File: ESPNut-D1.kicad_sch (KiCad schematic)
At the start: 53 parts, among them J1 USB_C_Receptacle_USB2.0, J2 ESP_CONN, J3 USB_PADS, J4 ESP_PROG, Q1 BC817, Q2 BC817, Q3 Si2302CDS, SW1 ESP_RST, SW2 ESP_BOOT, SW3 ESP_VDD_SW, SW4 POW_CTRL, U1 CH340G, U2 MIC5219-3.3YM5, Y1 12MHz

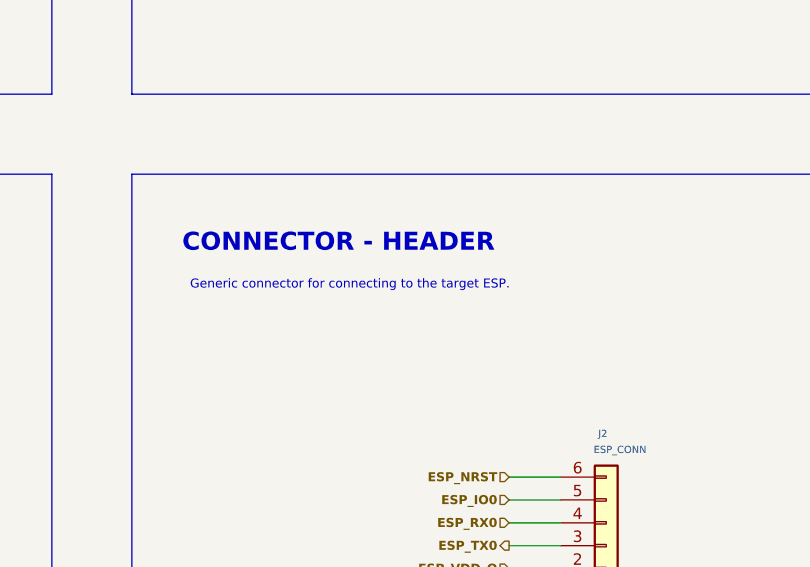
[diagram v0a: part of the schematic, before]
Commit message: Added fiducial
- Added fiducial to the front side.
- Generated new manufacturing files.
- Updated Readme.
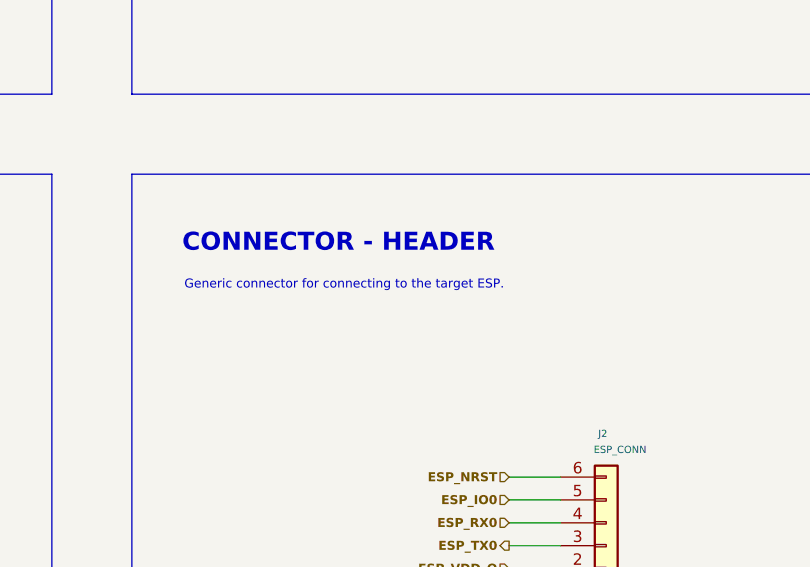
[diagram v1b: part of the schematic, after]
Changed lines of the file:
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@@
 	(title_block
 		(title "ESPNut-D1")
-		(date "2025-04-11")
+		(date "2025-04-23")
 		(rev "0.1")
 		(company "CIRCUITSTATE Electronics LLP (www.circuitstate.com)")
@@
 	(text_box "Generic connector for connecting to the target ESP."
 		(exclude_from_sim no)
-		(at 213.995 120.015 0)
+		(at 213.36 120.015 0)
 		(size 43.815 2.54)
 		(margins 0.7499 0.7499 0.7499 0.7499)
@@
 			"AGUAQQBkACsARABqADEAQQBKAHkAVwAzAFcAYgAxAEUAQgBFAC8ASAA3AG4ATQB6AGYARwBUAEEA"
 			"TQBBAFQAQgBkAGsAQQBBAEEAQQBBAEEAQQBBAEEAQQBBAEEAQQBBAEEAQQBBAEEAQQBCAHcASABt"
-			"ADYAVAB1AGQAawByAFgAeQBzAFMAMQA5AGYASgBmAFEANgBTAEwAQwBIACsATgBDACsAcgBqAA=="
+			"ADYAVAB1AGQAawByAFgAeQBzAFMAMQA5AGYASgBmAFEANgBTAEwAQwBIACsATgBDACsAcgBqAC8A"
+			"VAAvAEIAawBBAFAAZABwAHYAVgBRADMAVAA3AGUAMAB6AEUAWQBhAFgAYQBBAFAAQwBxAEgANgBj"
+			"AGUAQQBBAEEAQQBBAEEAQQBBAEEAQQBBAEEAQQBBAEEAQQBBAEEAQQBBAEEARQBqADcARwBoAEcA"
+			"ZgBFADcAbABGAC8ATAA0AGMATgAzAE4AZAAwADIAMgBjAHcAKwB3ADIAcQA0AGQANQBXAGQAMQBH"
+			"AHgASwBjADkAMABTAEkAaQB0AHQAOQA4AGIAcABIAGMAbwArADQANgAxADAAQwBjAG0AVABQADcA"
+			"VgB0AE4AdABuAE0ATwA4AGwAVABPAGIAbAA5AFUAcwBuAGcAbwBUAFAANwA0AFMAdQA5AHQAdABW"
+			"AHUAdQBoAFoANABFADkAcgBpAFAAaQBwADIAVAAyAGEAbAA1AFcATgAyADAAaABIAFEAQgBrAEwA"
+			"VAB0AGsAYgA5AG8ASABPAEUAeABtAFgAbABaADMARQBmAEgAbgBaAEwAdwBJAHAAYQB0ADAANQBP"
+			"ADgASwAwAEkAdAAxADUAUAA4AGUAOAB4AGcAUgBOADQATgBOAEEAcwBDADcAOQBjAFAAVQBBAHcA"
+			"QQBBAEEAQQBBAEEAQQBBAEEAQQBBAEEAQQBBAEEAQQBBAEEAQQBBAEIAcABUAFQASwAzAGUAUAA2"
+			"AGIAZQBWAGsAVgBpAFcAdAB1AFIAeQA3AHEAcgBCAE8AWgA0AHYAbAB2ADIAdgBLAHIARAA0AG4A"
+			"cgBiAHIAdQBQAE0ANQBnAG0AbQBWAHMAOAAvADQAMAB6AG0AMQBTAFQAegBDADIAZQAvADgAYQBa"
+			"AEQAYQBhAE8AaQBMADkARgB4AEYAOQBlACsAZgBqAEgAdgBLAHoAVwBJADgAMABUADgAWABvAEIA"
+			"SAArADkAVQBXADAATAA2AFMAegBMACsASQBTAEsAdQBCAGgAdQBtAG0ANAA5AFQARAA4AEMAZwBI"
+			"AHEAYwBlAGcASABkAHAATQBmAFUAQQBiADEAaQBSAHoATgAxAE8AWABZADQAZAA4AGQAdgBQAHgA"
+			"dQB3ADkANAAzAEsANABTAFgAagBEADYAdgBCADMAaABYAFAAMQBjAGUAbwBCAGUATgBJACsAKwBP"
+			"AHEAdgBzAGYAKwArADgAVABZAGkAQwBnAC8ANQBBAFcAQQBJAFAAMAA0ADkAQQBBAEEAQQBBAEEA"
+			"QQBBAEEAQQBBAEEAQQBBAEEAQQBBAEEAQQBBAEEASgBEAFcASgBIAE8ATABiADMANQBmAEoASwA2"
+			"AHAATwA4AHoAUgBoAHoAbwBpAC8AcgB3AG4AVQAzAHoAegArADEAbQBIAHQAVQA5AEYAawA4AHQA"
+			"cgBrAFkAagBmAHQAawBXADYAWQA2AHMAVABtAGUATABaAGYAOAA4AHkAaQAzAFkAcwBGAEIAeABE"
+			"AGsAdwBrADUAcwA1AFAAUwBaAEUATABPADcATQAyAHAATwAyAFMATABnAFcAWQA0AHgATABKAEQA"
+			"OQBtAEcAZwBHAFcAagB0AE4AcQB0AHQANQBJAHQAQQBMACsAWgBsAGQAVABuAFEASwBIAFcASABi"
+			"AEQASABRAEQASQBkAFkAZABzAGcAKwA5AEwAVABuAFgAVABMADMAKwBZAFMASwBIAEkAdABrAHIA"
+			"aAA1AHcAQgBvAFoAMwBqAHEAWABDAHkAMgBRAHUAOAB6AEEAUwBXAHUAMAA5ADUAMABVAHkAWABn"
+			"ADgAMwB5AGMARwAyAHkAZAB6AEYAcgAvAGYAWABjAEkATABxAEQAdABsAGkAbwBCAGsATwBzAGUA"
+			"eQBRAGYAZQBoAGgAdgA3AHAARAB0AHUAaABoAHYANwA0AHMATwAyAFMAYgBnAFcAWQBBAGcASABk"
+			"AEwAUQBUAFkAQQBBAEEAQQBBAEEAQQBBAEEAQQBBAEEAQQBBAEEAQQBBAEEAQQBDAGMAbAB6AHEA"
+			"WgBXADcAUwAvAEYAagAyAHUAMgBiAGYATQB2AHMAVwB6AC8ALwA2AFUAeQBIADgAOQBhAEoASgBo"
+			"ADEAYwBuAGMAbwB2ADIAMQA2AEgASABOAHYAbQBYADIATABaADcAOQB0AHoAUAByAHYAbQBiAGYA"
+			"TQB2AHMAVwB6AC8ANwA3AFgATQArAHMARAAzAGMAZABzAHAAYwBEAHoAWABDAEkAcQAyAHgAdwB0"
+			"ADEAbgBWAHcANAAzAEIATQA5AGMARABaAGIAdQA0ADYANQBDADkASABHAGkARwBRADEAeABsAGcA"
+			"egAyACsAbgA1AHMATwAyAFcAVgBQAGUAeAA2AHMATABWAFgALwBrAEkAegBmAEQAVABjAEoASQAy"
+			"AGkAUwB1AFkAdgBrAHcAegBvAEcATgBTACsAcgBXAFUAUgA4AFQAcwBhAGIANABTAFoANQBrADUA"
+			"WQBkAHMAdQB1AEIAWgBqAGoARwB1AGsATwAyAEcARwBnAEcATwBOAFoAZABoACsAegBsAFEARABN"
+			"AGMANABpAG8AYgA3AE8AbgBlADYAcQA1AEQAOQByAEsASAAvAGYAcAB5AG0AYwB6AGQAVAAvAFQA"
+			"ZwBLAHcAQgA0ADAAeABSAGsAQQB3AEEAQQBBAEEAQQBBAEEAQQBBAEEAQQBBAEEAQQBBAEEAQQBB"
+			"AHcASABsAHAAawByAGwAWgArADIAdQBSAHkATgBZAEgAegBOAEcASAB6AEwANgBmADUAbQBYAA=="
 		)
 	)

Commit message: New Revision `R0.2`
- Schematic
  - Deleted the Mosfet based power control circuit.
    - Replaced it with `AP22804AW5` based circuit.
    - Not because it is not working, but because a proper load switch is more reliable.
  - Added 6-pin `SM06B-SRSS-TB` JST-SH connector for target ESP.
    - The THT pin-headers will be changes to SMD one and placed on the back side.
  - Added `PCM12SMTR` SPDT switch for ESP voltage selection.
    - Removed the 3-pin solder jumper.
- PCB
  - Imported all changes to the PCB.
  - Deleted all existing tracks and vias.
  - Rearranged the components.
  - Updated label styles and placements.
  - There is now more alignment and symmetry.
  - Routing pending.
- New Revision `R0.2`.
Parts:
- removed D1, D4: RB751V40, Diode_SMD:D_SOD-323_HandSoldering, symbol Diode:MBR340
- removed D5: ESP_PWR, LED_SMD:LED_0603_1608Metric, symbol Device:LED
- removed JP3: VDD_CTRL_BYP, CSE_Solder-Jumper:Solder-Jumper-1x2_P1.3mm_Open_Rounded_1.0x1.2mm, symbol Jumper:SolderJumper_2_Open
- removed JP4: ESPV_SEL, CSE_Solder-Jumper:Solder-Jumper-1x3_P1.3mm_Open_Rounded_1.0x1.5mm_Labels, symbol Jumper:SolderJumper_3_Open
- removed Q3: Si2302CDS, Package_TO_SOT_SMD:SOT-23, symbol PCM_Transistor_MOSFET_AKL:Si2302CDS
- removed R8: 5.1K, Resistor_SMD:R_0402_1005Metric, symbol Device:R_Small
- removed R9: 220R, Resistor_SMD:R_0402_1005Metric, symbol Device:R_Small
- added D3: ESP_PWR, LED_SMD:LED_0603_1608Metric, symbol Device:LED
- added J3: ESP_CONN, CSE_Connector_JST_SH:JST_SH_SM06B-SRSS-TB_1x06-1MP_P1.00mm_Horizontal, symbol Connector_Generic:Conn_01x06
- added JP1: RST_PUE, CSE_Solder-Jumper:Solder-Jumper-1x2_P1.3mm_Open_Rounded_1.0x1.2mm, symbol Jumper:SolderJumper_2_Open
- added JP2: BT_PUE, CSE_Solder-Jumper:Solder-Jumper-1x2_P1.3mm_Open_Rounded_1.0x1.2mm, symbol Jumper:SolderJumper_2_Open
- added JP6: ESP_VDD_SW, CSE_Solder-Jumper:Solder-Jumper-1x2_P1.3mm_Open_Rounded_1.0x1.2mm, symbol Jumper:SolderJumper_2_Open
- added R10, R12, R3, R4: 10K, Resistor_SMD:R_0402_1005Metric, symbol Device:R_Small
- added R11, R13: 220R, Resistor_SMD:R_0402_1005Metric, symbol Device:R_Small
- added SW4: ESPV_SEL, Button_Switch_SMD:SW_SPDT_PCM12, symbol Switch:SW_SPDT
- added U3: AP22804AW5, Package_TO_SOT_SMD:SOT-23-5, symbol Power_Management:AP22804AW5
- J2: footprint Connector_PinHeader_2.54mm:PinHeader_1x06_P2.54mm_Vertical -> CSE_Solderpads:Solderpad_1x06_P2.54mm_Rounded_Rectangle
- JP5: value ESP_VDD_SW -> VDD_CTRL_BYP
- renumbered D2 to D1, D3 to D2, J3 to J4, J4 to J5, JP1 to JP3, JP2 to JP4, JP6 to JP7, R3 to R5, R4 to R6, R5 to R7, R6 to R8, R7 to R9, SW4 to SW5, TP8 to TP1, TP9 to TP2, TP1 to TP3, TP2 to TP4, TP3 to TP5, TP4 to TP6, TP5 to TP7, TP6 to TP8, TP7 to TP9
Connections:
- net +3V3: now also R3.1, R4.1, SW4.3 (C)
- net DTR: now also R11.2
- net ESP_IO0: now also Q2.3 (C), J3.5 (Pin_5), JP2.1 (A)
- net ESP_NRST: now also Q1.3 (C), J3.6 (Pin_6), JP1.1 (A)
- net ESP_RX0: now also J3.4 (Pin_4)
- net ESP_TX0: now also J3.3 (Pin_3)
- net ESP_VDD_I: now also JP5.2 (B), R10.2, R12.2, SW4.2 (B), U3.5 (IN)
- net ESP_VDD_O: now also D3.2 (A), J3.2 (Pin_2), JP6.1 (A); no longer JP5.1 (A)
- net GND: now also J3.1 (Pin_1), R13.1, U3.2 (GND)
- net VBUS: now also SW4.1 (A)
- net at TP11.1: now also D3.1 (K), R13.2
- net at JP7.2 (B), SW5.2: now also R10.1, R11.1, U3.4 (EN)
- net at SW3.1 (A): now also JP5.1 (A), JP6.2 (B), U3.1 (OUT); no longer JP5.2 (B)
- new net: JP2.2 (B), R4.2
- new net: R12.1, U3.3 (~{FLG})
- new net: JP1.2 (B), R3.2
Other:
- note added: "CH340G/C"
- note added: "JST-SH"
- note added: "Pin-Header"
- note removed: "CH340G"
- note removed: "Didoes are to prevent reverse voltage"
- moved on the sheet: C1, C2, C3, C4, C5, C6, H1, H2, J2, JP3, JP4, JP7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

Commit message: Routing completed
- Schematic
  - Updated BoM.
  - Reset the annotations.
- PCB
  - Imported all changes to the PCB.
  - Routing completed.
  - DRC passes.
  - Updated Fab layers.
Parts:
- D2: Name (none) -> TVS
- H1, H2: Name (none) -> Mounting Hole
- TP1: value CTS -> VBUS; Name CTS -> VBUS
- TP10: value CTS -> ESP_VDD_O; Name CTS -> ESP_VDD_O
- TP11: value CTS -> ESP_PWR_1; Name CTS -> ESP_PWR_1
- TP2: value CTS -> VBUS_LED_1; Name CTS -> VBUS_LED_1
- U1: Name (none) -> USB-Serial
- U2: Name 3.3V -> 3.3V LDO
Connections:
- net ESP_VDD_O: now also SW3.1 (A); no longer SW3.2 (B)
- net at JP5.1 (A), JP6.2 (B), U3.1 (OUT): now also SW3.2 (B); no longer SW3.1 (A)
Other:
- note added: "TARGET CONNECTORS"
- note added: "TARGET POWER CONTROL"
- note removed: "CONNECTOR - HEADER"
- note removed: "ESP VDD CONTROL"
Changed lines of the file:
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@@
 		)
 	)
-	(text "CONNECTOR - HEADER"
+	(text "TARGET CONNECTORS"
 		(exclude_from_sim no)
 		(at 213.868 118.11 0)
@@
 		)
 	)
-	(text "ESP VDD CONTROL"
+	(text "TARGET POWER CONTROL"
 		(exclude_from_sim no)
 		(at 308.102 117.856 0)
@@
 		)
 	)
-	(text_box "DTR is HIGH in idle conditions.\nWhen activated, it goes LOW and thus turns off the Mosfet."
+	(text_box "DTR is HIGH in idle conditions.\nWhen activated, it goes LOW."
 		(exclude_from_sim no)
-		(at 310.515 169.545 0)
-		(size 15.84 7.62)
+		(at 310.515 170.815 0)
+		(size 15.84 6.35)
 		(margins 0.5999 0.5999 0.5999 0.5999)
 		(stroke
@@
 		)
 	)
-	(text_box "If you don't have access to the ESP NRST pin,\nyou can use the DTR signal to disconnect the power\nto the ESP by removing the jumper and allowing\nthe Mosfet to control the supply to the ESP."
-		(exclude_from_sim no)
-		(at 308.01 120.2931 0)
-		(size 45.685 6.3509)
-		(margins 0.7499 0.7499 0.7499 0.7499)
-		(stroke
-			(width -0.0001)
-			(type default)
-		)
-		(fill
-			(type none)
-		)
-		(effects
-			(font
-				(size 1 1)
-				(color 74 187 255 1)
-			)
-			(justify left top)
-		)
-	)
 	(text_box "USB 2.0 to serial converter."
 		(exclude_from_sim no)
@@
 			)
 		)
-		(property "Name" ""
+		(property "Name" "USB-Serial"
 			(at 147.32 66.675 0)
 			(effects
@@
 			)
 		)
-		(property "Value" "CTS"
+		(property "Value" "VBUS"
 			(at 67.056 46.4819 0)
 			(effects
@@
 			)
 		)
-		(property "Name" "CTS"
+		(property "Name" "VBUS"
 			(at 66.04 46.355 0)
 			(effects
@@
 			)
 		)
+		(property "Name" "Mounting Hole"
+			(at 144.145 241.3 0)
+			(effects
+				(font
+					(size 1.27 1.27)
+				)
+				(hide yes)
+			)
+		)
 		(instances
 			(project "ESPNut-D1"
@@
 			)
 		)
-		(property "Name" ""
+		(property "Name" "TVS"
 			(at 75.565 73.025 0)
 			(effects
@@
 			)
 		)
+		(property "Name" "Mounting Hole"
+			(at 144.145 234.315 0)
+			(effects
+				(font
+					(size 1.27 1.27)
+				)
+				(hide yes)
+			)
+		)
 		(instances
 			(project ""
@@
 		(lib_id "Switch:SW_SPST")
 		(at 361.315 149.225 0)
+		(mirror y)
 		(unit 1)
 		(exclude_from_sim no)
@@
 		(dnp no)
 		(property "Reference" "SW3"
-			(at 360.553 143.51 0)
+			(at 360.807 143.51 0)
 			(effects
 				(font
@@
 		)
 		(property "Value" "ESP_VDD_SW"
-			(at 360.553 145.288 0)
+			(at 360.807 145.288 0)
 			(effects
 				(font
@@
 			)
 		)
-		(property "Value" "CTS"
+		(property "Value" "ESP_PWR_1"
 			(at 369.316 166.4969 0)
 			(effects
@@
 			)
 		)
-		(property "Name" "CTS"
+		(property "Name" "ESP_PWR_1"
 			(at 368.3 166.37 0)
 			(effects
@@
 			)
 		)
-		(property "Value" "CTS"
+		(property "Value" "VBUS_LED_1"
 			(at 77.216 46.4819 0)
 			(effects
@@
 			)
 		)
-		(property "Name" "CTS"
+		(property "Name" "VBUS_LED_1"
 			(at 76.2 46.355 0)
 			(effects
@@
 			)
 		)
-		(property "Name" "3.3V"
+		(property "Name" "3.3V LDO"
 			(at 135.89 146.05 0)
 			(effects
@@
 			)
 		)
-		(property "Value" "CTS"
+		(property "Value" "ESP_VDD_O"
 			(at 369.316 154.4319 0)
 			(effects
@@
 			)
 		)
-		(property "Name" "CTS"
+		(property "Name" "ESP_VDD_O"
 			(at 368.3 154.305 0)
 			(effects

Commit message: New Revision `R0.3` - Schematic   - Added DPDT `UART_SWAP` switch to swap the `TX` and `RX` lines.     - But this is DNPed because the switch consumes too much space.   - Added UART activity LEDs on both `TX` and `RX` lines.   - Changed all existing transistor footprints to `SOT-523`.   - Excluded `AP22804AW5`'s `FLG` resistor from the board.   - Updated the BoM.   - Reset the annotations. - PCB   - Imported all changes to the PCB.   - Updated placements.   - Routing completed.   - Updated Fab layers.   - DRC passes. - Generated manufacturing files. - Schematic   - Added `DIFF` class for differential pairs.   - Added `1K` series resistors to both the `TX` and `RX` lines.     - This will limit the current and reverse voltage to the target.     - Previously we only had a single `220R` resistor on the `RX` line of the `CH340`.     - A value of `1K` does not affect performance. - New Revision 🆕 `R0.3`.
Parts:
- added D4: RX_LED, LED_SMD:LED_0603_1608Metric, symbol Device:LED
- added D5: TX_LED, LED_SMD:LED_0603_1608Metric, symbol Device:LED
- added Q3, Q4: MMBT3906T-7-F, CSE_Package_TO_SOT_SMD:SOT-523, symbol Transistor_BJT:MMBT3906
- added R15, R16, R6: 1K, Resistor_SMD:R_0402_1005Metric, symbol Device:R_Small
- added R17, R18: 220R, Resistor_SMD:R_0402_1005Metric, symbol Device:R_Small
- added SW6: UART_SWAP, Button_Switch_THT:SW_CuK_JS202011CQN_DPDT_Straight, symbol Switch:SW_Slide_DPDT
- Q1, Q2: value BC817 -> MMBT3904T-7-F; footprint Package_TO_SOT_SMD:SOT-23 -> CSE_Package_TO_SOT_SMD:SOT-523; MFR Nexperia -> Diodes Incorporated; MPN BC817-16,215 -> MMBT3904T-7-F
- R13: renamed from R12; now left out of the parts list
- R8: renamed from R7; value 220R -> 1K; MFR Yageo -> Walsin; MPN RC0402FR-7D220RL -> WR04X1001FTL
- SW1, SW2, SW5: Alt MPN (none) -> BX-TS-26-3425TP; MFR USAKRO -> XUNPU; MPN UK-B0273-SP25Y -> TS-1088R-02526
- U1: Alt MPN (none) -> CH340C
- renumbered J4 to J2, J2 to J3, J3 to J4, R9 to R10, R10 to R11, R11 to R12, R13 to R14, R6 to R7, R8 to R9
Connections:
- net ESP_VDD_O: now also Q3.3 (C), Q4.3 (C)
- net GND: now also D4.1 (K), D5.1 (K)
- net ESP_RX0 renamed CH_TX
- net CH_TX: now also R15.2, R6.1, SW6.1 (A), SW6.2 (B), SW6.4 (A); no longer U1.2 (TXD)
- net ESP_TX0 renamed CH_RX
- net CH_RX: now also R16.2, SW6.3 (C), SW6.5 (B), SW6.6 (C)
- new net: Q4.1 (B), R16.1
- new net: Q4.2 (E), R18.1
- new net: Q3.1 (B), R15.1
- new net: Q3.2 (E), R17.1
- new net: D4.2 (A), R17.2
- new net: D5.2 (A), R18.2
- new net: R6.2, U1.2 (TXD)
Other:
- note added: "UART LEDs"
- note added: "UART SWAP SWITCH"
- note removed: "MOUNTING HOLES"
- moved on the sheet: H1, H2, J2

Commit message: Updated BoM
- Updated BoM.
  - Fixed UART activity LEDs MPNs.
- Generated new manufacturing files.
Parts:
- D4: MPN 19-21SURC/S530-A2/TR8 -> 19-213/BHC-ZL1M2RY/3T; Name VBUS_LED -> RX_LED
- D5: MPN 19-21SURC/S530-A2/TR8 -> 19-217/R6C-AL1M2VY/3T; Name VBUS_LED -> TX_LED
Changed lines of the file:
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@@
 			)
 		)
-		(property "Name" "VBUS_LED"
+		(property "Name" "RX_LED"
 			(at 229.235 252.73 0)
 			(effects
@@
 			)
 		)
-		(property "MPN" "19-21SURC/S530-A2/TR8"
+		(property "MPN" "19-213/BHC-ZL1M2RY/3T"
+			(at 229.235 252.73 0)
+			(effects
+				(font
+					(size 1.27 1.27)
+				)
+				(hide yes)
+			)
+		)
+		(property "Class" ""
 			(at 229.235 252.73 0)
 			(effects
@@
 			)
 		)
-		(property "Name" "VBUS_LED"
+		(property "Name" "TX_LED"
 			(at 258.445 252.73 0)
 			(effects
@@
 			)
 		)
-		(property "MPN" "19-21SURC/S530-A2/TR8"
+		(property "MPN" "19-217/R6C-AL1M2VY/3T"
+			(at 258.445 252.73 0)
+			(effects
+				(font
+					(size 1.27 1.27)
+				)
+				(hide yes)
+			)
+		)
+		(property "Class" ""
 			(at 258.445 252.73 0)
 			(effects

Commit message: Added `47 uF` 0805 capacitors
- Schematic
  - Added `47 uF` 0805 capacitors to the VBUS line, near the CH340 and `ESP_VDD_I`.
    - This was required because it was observed that the CH340 will reset when a significant load is connected to the `VBUS` line.
    - Adding two 22 uF capacitors proved to solve the issue.
    - But we are going to use 47 uF capacitors for better stability.
- PCB
  - Imported all changes to the PCB.
  - DRC passes.
- No version changes.
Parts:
- added C1, C8: 47uF, Capacitor_SMD:C_0805_2012Metric, symbol Device:C_Small
- renumbered C1 to C2, C2 to C3, C3 to C4, C4 to C5, C5 to C6, C6 to C7, J3 to J2, J4 to J3, J2 to J4
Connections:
- net ESP_VDD_I: now also C8.1
- net GND: now also C1.1, C8.2
- net VBUS: now also C1.2
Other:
- moved on the sheet: C3, C4, C5, C6, C7, SW4, U2

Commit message: New Revision 🆕 `R0.4`
- Schematic
  - Removed the PNP transistors from the UART activity LED circuit.
    - The SparkFun Serial Basic directly connects the LEDs to the TX and RX lines via `1K` resistors.
    - We will do the same.
    - But the voltage supplied to the LEDs can be set using a jumper `ACT-LED-V`.
  - Added jumper `TRX-PUV` to the CH340 communication lines.
    - This jumper selects between `ESP_VDD_I` and `ESP_VDD_O` for the pull-ups.
  - ERC passes.
- PCB
  - Imported all changes to the PCB.
  - Placement and routing completed.
  - DRC passes.
- This will be a test version and aesthetics don't matter now.
- Generated manufacturing files.
- New Revision 🆕 `R0.4`.
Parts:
- removed Q3, Q4: MMBT3906T-7-F, CSE_Package_TO_SOT_SMD:SOT-523, symbol Transistor_BJT:MMBT3906
- removed R17, R18: 220R, Resistor_SMD:R_0402_1005Metric, symbol Device:R_Small
- removed R6, R8: 1K, Resistor_SMD:R_0402_1005Metric, symbol Device:R_Small
- removed R9: DNP, Resistor_SMD:R_0402_1005Metric, symbol Device:R_Small
- added D2: BAS70K, Diode_SMD_AKL:D_SOD-523, symbol Diode_Schottky_AKL:BAS70K
- added JP3: TRX-PUV, CSE_Solder-Jumper:Solder-Jumper_1x3_0402_Open, symbol Jumper:SolderJumper_3_Open
- added JP9: ACT-LED-V, CSE_Solder-Jumper:Solder-Jumper_1x3_0402_Open, symbol Jumper:SolderJumper_3_Open
- added Q2: 2SK3019-TP, CSE_Package_TO_SOT_SMD:SOT-523, symbol Transistor_MOSFET_AKL:2SK3018
- added R3: 10K, Resistor_SMD:R_0402_1005Metric, symbol Device:R_Small
- renumbered D2 to D3, D3 to D4, D4 to D5, D5 to D6, JP3 to JP4, JP4 to JP5, JP5 to JP6, JP6 to JP7, JP7 to JP8, Q2 to Q3, R12 to R10, R13 to R11, R14 to R12, R15 to R13, R16 to R14, R3 to R4, R4 to R5, R5 to R6, R10 to R8, R11 to R9
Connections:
- net +3V3: now also JP9.1 (A)
- net CH_RX: now also Q2.2 (S)
- net CH_TX: now also D2.2 (A), R3.2
- net ESP_VDD_I: now also JP3.3 (B), JP9.3 (B)
- net ESP_VDD_O: now also JP3.1 (A)
- net GND: no longer D5.1 (K), D6.1 (K)
- net at U1.3 (RXD): now also Q2.3 (D)
- net at R14.1: now also D6.1 (K)
- net at R13.1: now also D5.1 (K)
- net at D5.2 (A): now also D6.2 (A), JP9.2 (C)
- net at U1.2 (TXD): now also D2.1 (K)
- new net: JP3.2 (C), Q2.1 (G), R3.1
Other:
- note removed: "Shouldn't be used for ESP8266"
- moved on the sheet: C1, C2, C3, D5, D6, R13, R14, TP3, TP4, TP5, TP6, TP7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
